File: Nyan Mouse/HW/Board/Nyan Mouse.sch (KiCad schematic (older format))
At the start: 4 parts

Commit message: A lot of kicad.... A LOT.
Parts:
- added C?: 470uF, symbol CP1
- added C?: 100uF, symbol CP1
- added P?: CONN_20X2, symbol CONN_20X2
- added R?: 10k, symbol R
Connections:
- net labels added: drva1, drva2, drvb1, drvb2, sens1, sens2, sens3, sens4, sens5, sens6
- wire segments 14 -> 55
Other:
- note added: ""Connectors" for ground plane common reference point"
- moved on the sheet: M?

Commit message: Made changes to board 20% done still. :/
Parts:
- added U? (x2): DRV8837, symbol DRV8837
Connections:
- net labels added: re1, re2, re3, re4, re5, re6, re[1..6]
- net labels removed: drva1, drva2, drvb1, drvb2, sens1, sens2, sens3, sens4, sens5, sens6
- wire segments 55 -> 85
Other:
- note added: "Flip Flop Clock"
- note added: "SCK"
- note added: "SDI"
- note added: "drva1"
- note added: "drva2"
- note added: "drvb1"
- note added: "drvb2"
- note added: "~output enable"
- moved on the sheet: R?

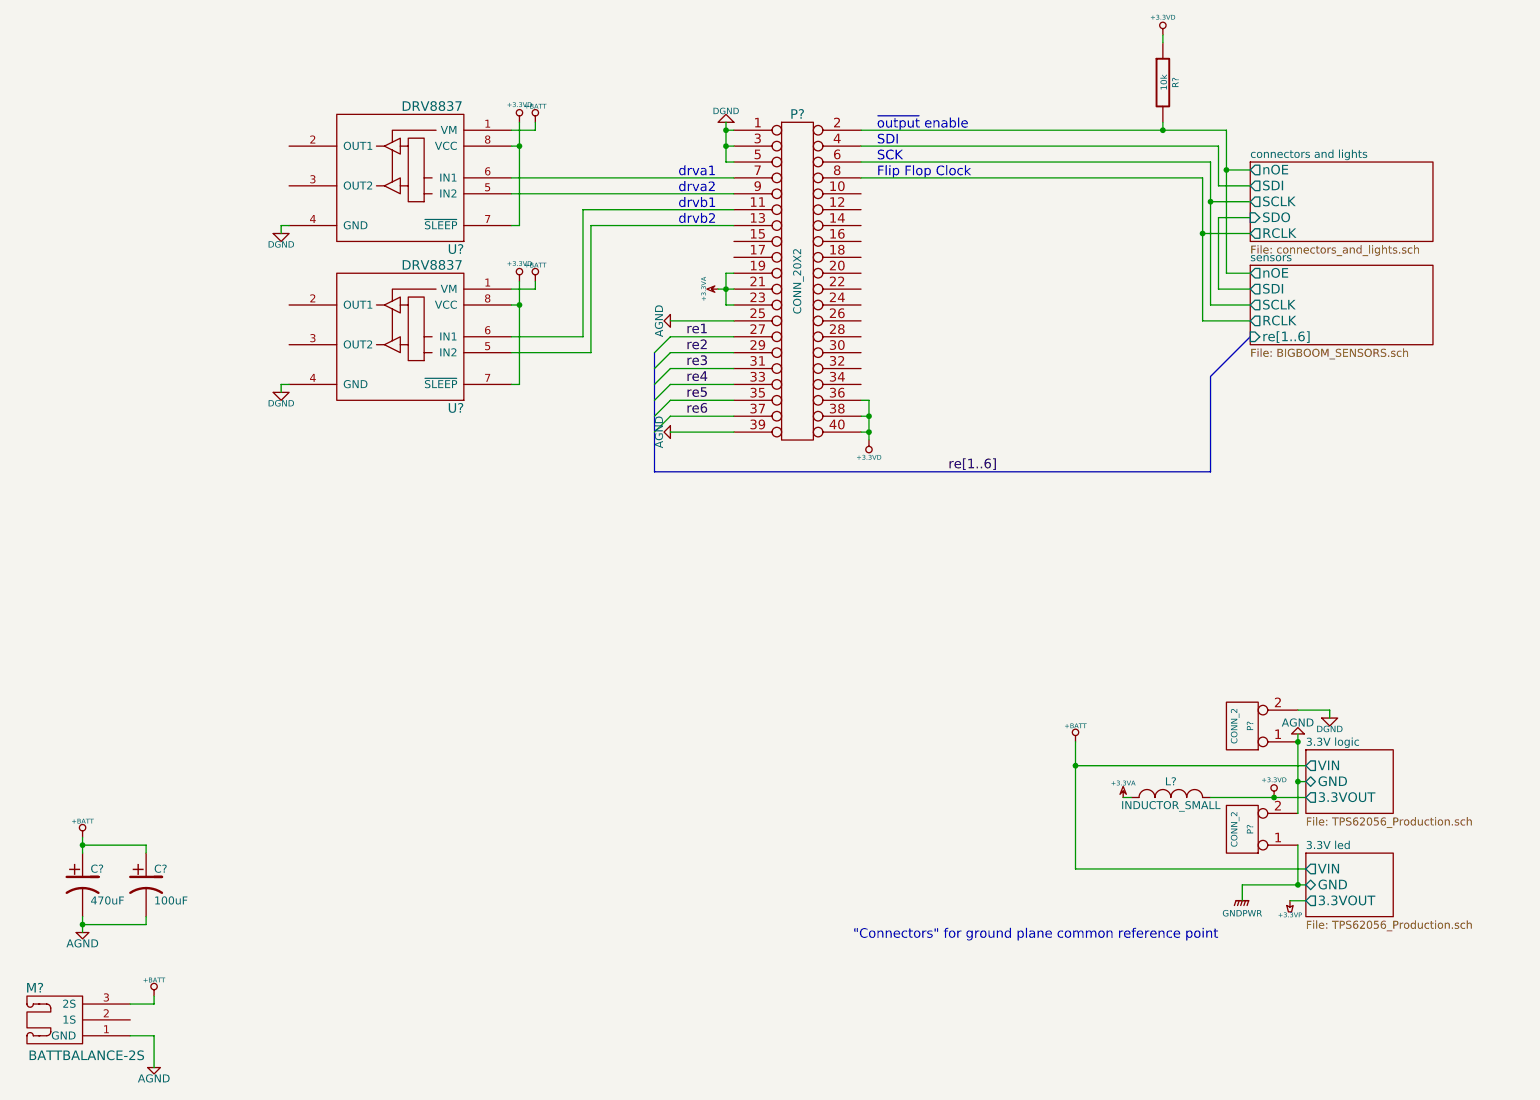
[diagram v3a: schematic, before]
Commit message: Changed DRV8837, Almost completed main board. ERC almost successful.
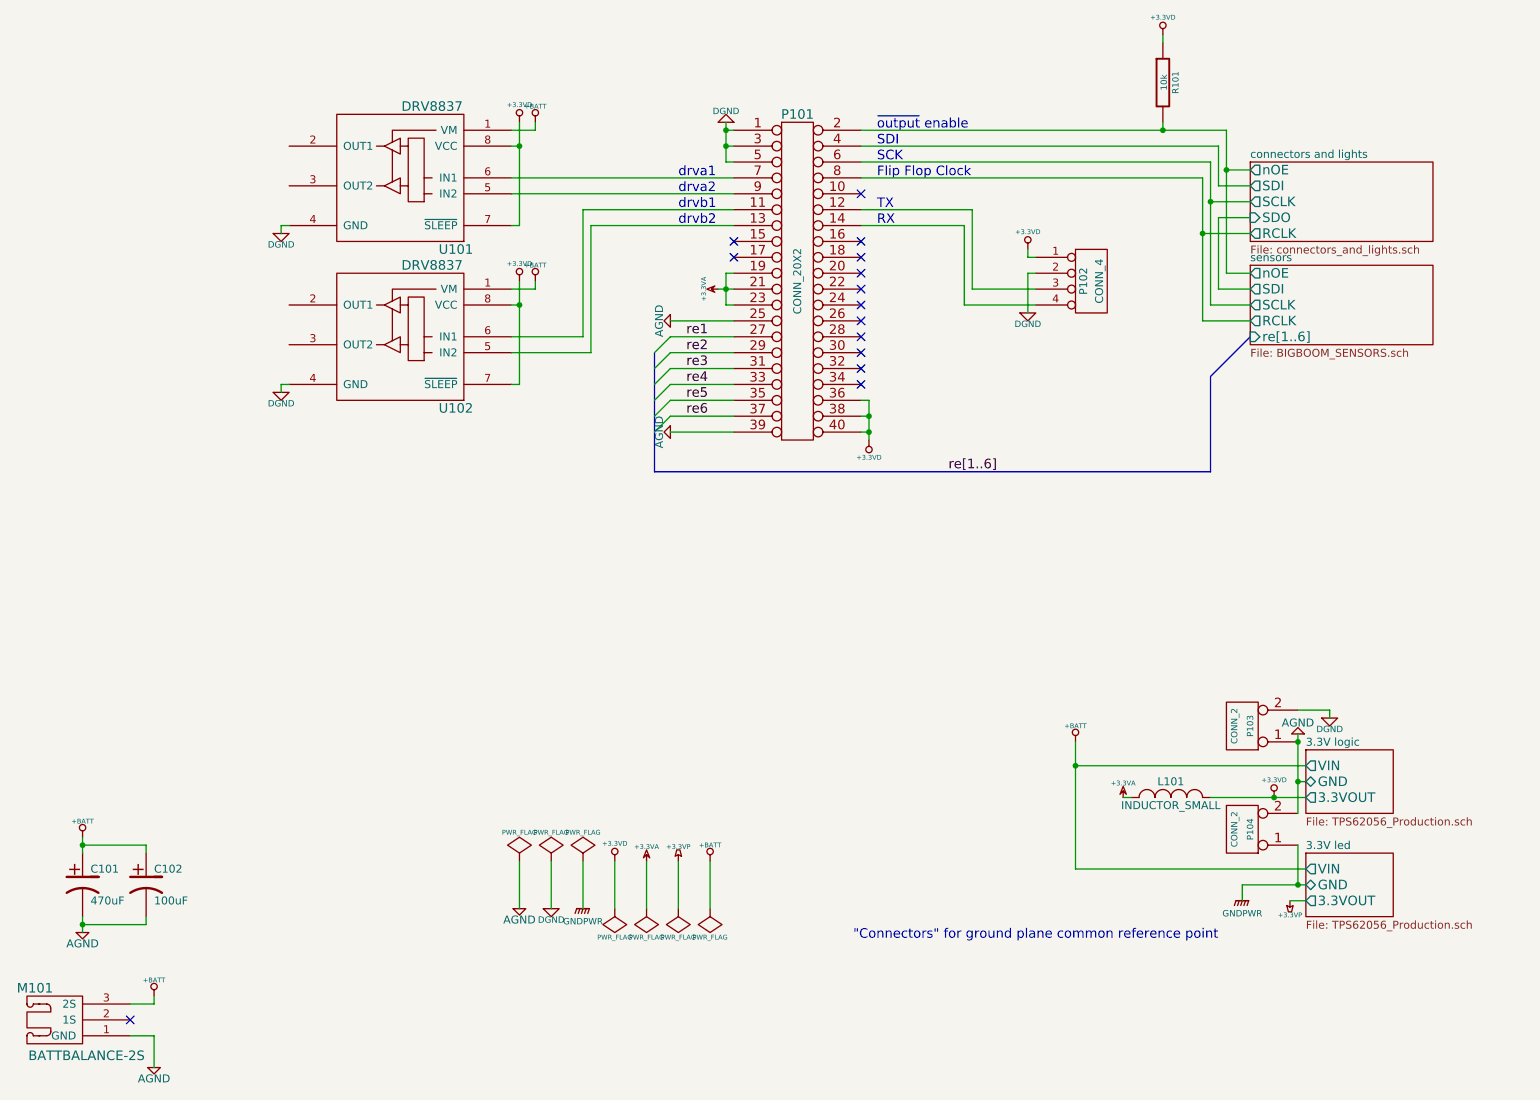
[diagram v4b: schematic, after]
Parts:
- added P102: CONN_4, symbol CONN_4
- gave numbers to parts that had none: 10
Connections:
- net +3.3VD: now also P102.1 (P1)
- net DGND: now also P102.2 (P2)
- net at P101.12 (P12): now also P102.3 (P3)
- net at P101.14 (P14): now also P102.4 (P4)
- no-connect marks 0 -> 14
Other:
- note added: "RX"
- note added: "TX"
